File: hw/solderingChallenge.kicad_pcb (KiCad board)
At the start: 2 copper layers, 119 x 40.7 mm, 30 parts, among them J2 USB_A, U1 LM555xN, U10 USB_A, U11 1k, U12 USB_A, U13 330R, U14 1k, U15 4.7u, U2 LMC555xM, U3 LMC555xMM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

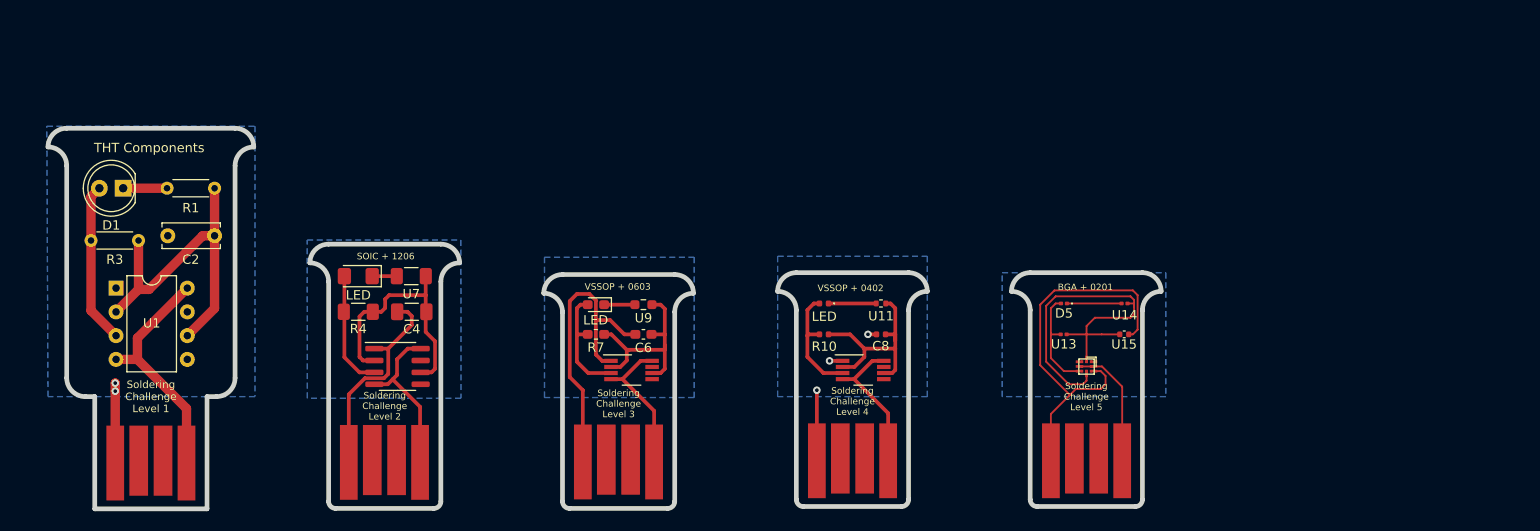
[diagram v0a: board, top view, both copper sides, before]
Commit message: Aesthetics
- resizing levels 2 and 3
- centering 555
- create the same labels for the same parts in all levels
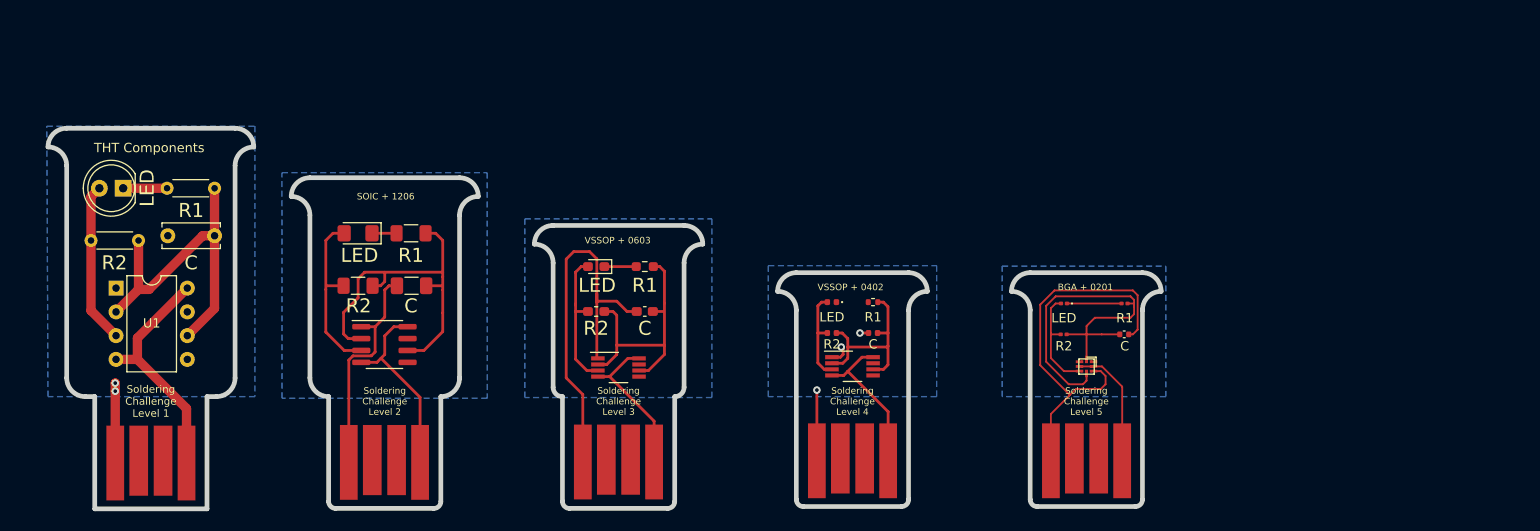
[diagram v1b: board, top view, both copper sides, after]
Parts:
- moved D2 4.58 mm to (114.2, 82.5)
- moved U7 4.58 mm to (119.8, 82.5)
- moved U9 4.07 mm to (144.8, 86.1)
- moved D3 4.07 mm to (139.6, 86.1)
- moved C4 2.78 mm to (119.9, 88.2)
- moved R4 2.78 mm to (114.2, 88.2)
- moved U2 2.73 mm to (117.0, 94.4)
- moved C6 2.45 mm to (144.8, 90.9)
- moved R7 2.45 mm to (139.6, 90.9)
- moved U3 1.42 mm to (142.0, 96.9)
- moved U4 1.21 mm to (167.0, 96.8)
- moved U11 0.87 mm to (169.2, 89.9)
- moved C8 0.87 mm to (169.2, 93.2)
- moved D4 0.86 mm to (164.8, 89.9)
- moved R10 0.86 mm to (164.8, 93.2)
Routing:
- net Net-(C4-Pad1): track 26.7 -> 38.7 mm
- net /Level 3 - 0603/GND: track 33.7 -> 42.7 mm
- net Net-(C6-Pad1): track 21.7 -> 28.1 mm
- net Net-(D2-Pad2): track 12.5 -> 18.5 mm
- net Net-(D4-Pad1): track 5.10 -> 0.00 mm
- net /Level 2 - 1206/VCC: track 17.6 -> 20.6 mm
- net Net-(D3-Pad2): track 12.3 -> 15.2 mm
- net Net-(D4-Pad2): track 12.4 -> 10.1 mm
- net Net-(C8-Pad1): track 22.3 -> 20.2 mm
- net /Level 2 - 1206/GND: track 22.8 -> 24.1 mm
- net /Level 4 - 0402/VCC: track 15.4 -> 16.6 mm
- net /Level 3 - 0603/VCC: track 15.5 -> 16.3 mm
- net /Level 4 - 0402/GND: track 9.86 -> 10.7 mm
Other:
- outline, holes or cut-outs redrawn
- board text added: "C"
- board text added: "LED"
- board text added: "R1"
- board text added: "R2"

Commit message: level 1
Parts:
- added Klobouek1: redhatLogo, Robotarna_KiCad_Library:RedhatLogo, B.Cu at (92.0, 77.0)
- added Kolecko1: robotarnaLogo, Robotarna_KiCad_Library:RobotarnaLogo-6mm, F.Cu at (89.5, 80.5)
- added R2: 1M, Resistor_THT:R_Axial_DIN0207_L6.3mm_D2.5mm_P15.24mm_Horizontal, F.Cu at (83.5, 84.5)
- C1: renamed from C2; value 4.7u -> 1u; footprint Capacitor_THT:C_Disc_D6.0mm_W2.5mm_P5.00mm -> Capacitor_THT:C_Disc_D7.5mm_W2.5mm_P5.00mm
- R1: value 1k -> 470; footprint Resistor_THT:R_Axial_DIN0204_L3.6mm_D1.6mm_P5.08mm_Horizontal -> Resistor_THT:R_Axial_DIN0207_L6.3mm_D2.5mm_P15.24mm_Horizontal
- R3: value 330 -> 470; footprint Resistor_THT:R_Axial_DIN0204_L3.6mm_D1.6mm_P5.08mm_Horizontal -> Resistor_THT:R_Axial_DIN0207_L6.3mm_D2.5mm_P15.24mm_Horizontal
- moved C4 38.0 mm to (157.9, 88.2)
- moved U2 38.0 mm to (155.0, 94.4)
- moved U6 38.0 mm to (155.0, 111.9)
- moved C6 38.0 mm to (182.8, 90.9)
- moved C8 38.0 mm to (207.2, 93.2)
- moved D2 38.0 mm to (152.2, 82.5)
- moved D3 38.0 mm to (177.6, 86.1)
- moved D4 38.0 mm to (202.8, 89.9)
- moved D5 38.0 mm to (227.6, 90.0)
- moved R10 38.0 mm to (202.8, 93.2)
- moved R4 38.0 mm to (152.2, 88.2)
- moved R7 38.0 mm to (177.6, 90.9)
- moved U10 38.0 mm to (205.0, 111.8)
- moved U11 38.0 mm to (207.2, 89.9)
- moved U12 38.0 mm to (230.0, 111.8)
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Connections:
- C1 pad 1: Net-(C2-Pad1) -> Net-(C1-Pad1)
- R1 pad 1: Net-(C2-Pad1) -> /Level 1 - THT/VCC
- R3 pad 1: Net-(D1-Pad2) -> Net-(D1-Pad1)
- R3 pad 2: Net-(C2-Pad1) -> /Level 1 - THT/GND
- U1 pad 2: Net-(C2-Pad1) -> Net-(C1-Pad1)
- U1 pad 6: Net-(C2-Pad1) -> Net-(C1-Pad1)
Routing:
- net Net-(C1-Pad1): track 0.00 -> 37.9 mm
- net Net-(C2-Pad1): track 36.1 -> 0.00 mm
- net Net-(D1-Pad2): track 17.2 -> 30.0 mm
- net /Level 1 - THT/VCC: track 25.4 -> 33.3 mm
- net Net-(D1-Pad1): track 4.69 -> 8.66 mm
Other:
- board size 119 x 40.7 mm -> 159 x 50.5 mm
- board text added: "R3"

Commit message: Level 2 and 3
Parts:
- removed C4: 4.7u, Capacitor_SMD:C_1206_3216Metric_Pad1.33x1.80mm_HandSolder
- removed C6: 4.7u, Capacitor_SMD:C_0603_1608Metric_Pad1.08x0.95mm_HandSolder
- removed C8, U15: 4.7u, Capacitor_SMD:C_0402_1005Metric
- removed D4: LED, LED_SMD:LED_0402_1005Metric
- removed D5: LED, LED_SMD:LED_0201_0603Metric
- removed R10: 330R, Resistor_SMD:R_0402_1005Metric
- removed R7: 330R, Resistor_SMD:R_0603_1608Metric_Pad1.05x0.95mm_HandSolder
- removed U10, U12: USB_A, Robotarna_KiCad_Library:usb-PCB
- removed U11: 1k, Resistor_SMD:R_0402_1005Metric
- removed U13: 330R, Resistor_SMD:R_0201_0603Metric
- removed U14: 1k, Resistor_SMD:R_0201_0603Metric
- removed U4: LMC555xMM, Package_SO:VSSOP-8_3.0x3.0mm_P0.65mm
- removed U5: LMC555xTP, Package_BGA:Texas_DSBGA-8_1.43x1.41mm_Layout3x3_P0.5mm
- removed U7: 1k, Resistor_SMD:R_1206_3216Metric_Pad1.30x1.75mm_HandSolder
- removed U9: 1k, Resistor_SMD:R_0603_1608Metric_Pad0.98x0.95mm_HandSolder
- added C1: 1uF, Capacitor_SMD:C_0603_1608Metric_Pad1.08x0.95mm_HandSolder, F.Cu at (177.5, 92.3)
- added C2: 1u, Capacitor_SMD:C_1206_3216Metric_Pad1.33x1.80mm_HandSolder, F.Cu at (151.9, 80.7)
- added Klobouek1: redhatLogo, Robotarna_KiCad_Library:RedhatLogo, B.Cu at (180.0, 87.3)
- added Klobouek1: redhatLogo, Robotarna_KiCad_Library:RedhatLogo, B.Cu at (155.1, 82.8)
- added Kolecko1: robotarnaLogo, Robotarna_KiCad_Library:RobotarnaLogo-6mm, B.Cu at (180.0, 106.8)
- added Kolecko1: robotarnaLogo, Robotarna_KiCad_Library:RobotarnaLogo-6mm, B.Cu at (154.8, 106.9)
- added R2: 1M, Resistor_SMD:R_0603_1608Metric_Pad0.98x0.95mm_HandSolder, F.Cu at (182.3, 92.4)
- added R3: 470R, Resistor_SMD:R_1206_3216Metric_Pad1.30x1.75mm_HandSolder, F.Cu at (158.5, 80.7)
- added R5: 470R, Resistor_SMD:R_1206_3216Metric_Pad1.30x1.75mm_HandSolder, F.Cu at (155.9, 86.8)
- added R5: 470, Resistor_SMD:R_0603_1608Metric_Pad0.98x0.95mm_HandSolder, F.Cu at (182.3, 88.3)
- added R6: 470, Resistor_SMD:R_0603_1608Metric_Pad0.98x0.95mm_HandSolder, F.Cu at (177.5, 88.3)
- Kolecko1: moved to B.Cu
- R4: value 330R -> 1M
- moved Kolecko1 45.3 mm to (126.2, 107.0), turned to 180 degrees
- moved Klobouek1 37.6 mm to (129.6, 76.3)
- moved D1 34.2 mm to (125.0, 69.4)
- moved J2 34.2 mm to (126.2, 112.1)
- moved R1 34.2 mm to (129.7, 84.6)
- moved R2 34.2 mm to (117.7, 84.6)
- moved R3 34.2 mm to (133.7, 69.4)
- moved U1 34.2 mm to (118.9, 87.8)
- moved C1 34.2 mm to (133.7, 90.6)
- moved D2 8.97 mm to (160.1, 86.7), turned to -90 degrees
- moved D3 2.75 mm to (180.0, 84.7), turned to 0 degrees
- moved R4 1.65 mm to (151.2, 86.8), turned to -90 degrees
- moved U2 0.26 mm to (154.8, 94.6)
- moved U6 0.26 mm to (154.8, 112.1)
- moved U3 0.20 mm to (180.0, 97.1)
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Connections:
- D3 pad 2: Net-(D3-Pad2) -> (no net)
- R4 pad 1: Net-(C4-Pad1) -> (no net)
- U2 pad 2: Net-(C4-Pad1) -> (no net)
- U2 pad 6: Net-(C4-Pad1) -> (no net)
- U3 pad 2: Net-(C6-Pad1) -> (no net)
- U3 pad 3: Net-(D3-Pad2) -> (no net)
- U3 pad 6: Net-(C6-Pad1) -> (no net)
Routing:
- net (no net): track 0.00 -> 59.6 mm
- net /Level 5 - 0201/GND: track 41.6 -> 0.00 mm
- net Net-(U13-Pad1): track 39.6 -> 0.00 mm
- net Net-(C4-Pad1): track 38.7 -> 0.00 mm
- net Net-(C6-Pad1): track 28.1 -> 0.00 mm
- net /Level 2 - 1206/GND: track 24.1 -> 50.9 mm
- net /Level 2 - 1206/VCC: track 20.6 -> 41.7 mm
- net Net-(C8-Pad1): track 20.2 -> 0.00 mm
- net /Level 3 - 0603/GND: track 42.7 -> 25.3 mm
- net /Level 4 - 0402/VCC: track 16.6 -> 0.00 mm
- net Net-(D3-Pad2): track 15.2 -> 0.00 mm
- net /Level 5 - 0201/VCC: track 13.1 -> 0.00 mm
- net /Level 3 - 0603/VCC: track 16.3 -> 28.1 mm
- net Net-(D5-Pad2): track 11.3 -> 0.00 mm
- net /Level 4 - 0402/GND: track 10.7 -> 0.00 mm, vias 3 -> 0
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- removed copper zone on B.Cu, net /Level 4 - 0402/GND
- removed copper zone on B.Cu, net /Level 5 - 0201/GND
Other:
- board size 159 x 50.5 mm -> 75.8 x 50.6 mm
- board text removed: "BGA + 0201"
- board text removed: "L4"
- board text removed: "L5"
- board text removed: "Soldering Challenge Level 4"
- board text removed: "Soldering Challenge Level 5"
- board text removed: "VSSOP + 0402"

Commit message: Loga
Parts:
- removed Klobouek1 (x3): redhatLogo, Robotarna_KiCad_Library:RedhatLogo
- added G***: LOGO, LOGO, B.Cu at (180.0, 87.0)
- added G***: LOGO, LOGO, B.Cu at (126.0, 74.5)
- added G***: LOGO, LOGO, B.Cu at (154.8, 83.2)
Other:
- board text added: "RoboticsBrno"
- board text added: "Soldering Challenge Level 1 V2"
- board text added: "Soldering Challenge Level 2 V2"
- board text added: "Soldering Challenge Level 3 V2"
- board text added: "research.redhat.com"
- board text added: "smd-challenge. robotikabrno.cz"
- board text removed: "RoboticsBrno v1"
- board text removed: "Soldering Challenge Level 1"
- board text removed: "Soldering Challenge Level 2"
- board text removed: "Soldering Challenge Level 3"
